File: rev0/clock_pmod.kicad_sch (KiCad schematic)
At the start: 5 parts, among them IC1 ECP5-BGA256, Y1 Osc60MHz

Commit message: hardware: use DNP field for DNP notation
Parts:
- TP1: DNP (none) -> DNP; Note DNP -> (none)
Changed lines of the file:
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@@
       (effects (font (size 1.27 1.27)) hide)
     )
-    (property "Note" "DNP" (id 4) (at 118.11 142.24 0)
+    (property "DNP" "DNP" (id 4) (at 118.11 142.24 0)
       (effects (font (size 1.27 1.27)) hide)
     )

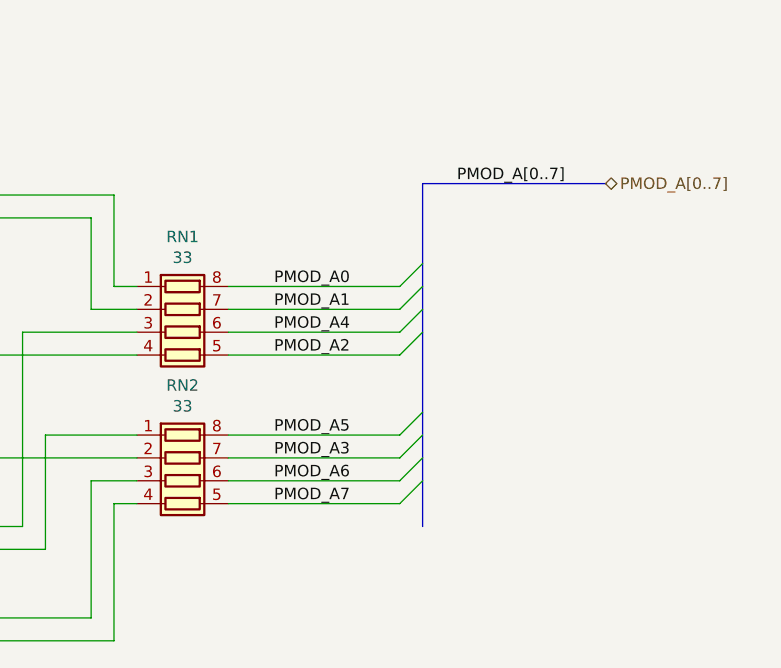
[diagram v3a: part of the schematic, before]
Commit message: hardware: reassign FPGA I/O banks
assign HyperRAM to DQS group
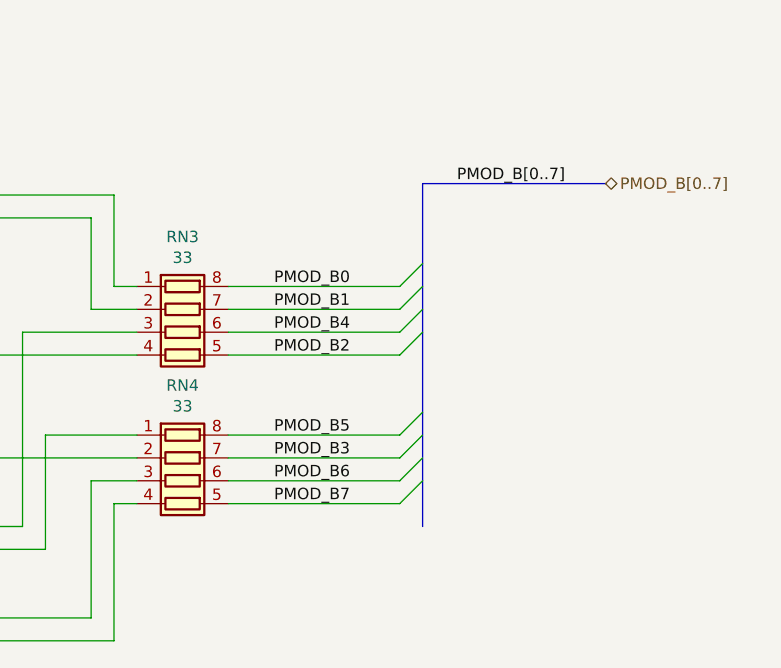
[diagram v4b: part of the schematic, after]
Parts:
- renumbered RN1 to RN3, RN2 to RN4
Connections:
- net PMOD_A0 renamed PMOD_B0
- net PMOD_A1 renamed PMOD_B1
- net PMOD_A2 renamed PMOD_B2
- net PMOD_A3 renamed PMOD_B3
- net PMOD_A4 renamed PMOD_B4
- net PMOD_A5 renamed PMOD_B5
- net PMOD_A6 renamed PMOD_B6
- net PMOD_A7 renamed PMOD_B7
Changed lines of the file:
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@@
     (stroke (width 0) (type default) (color 0 0 0 0))
   )
-  (label "PMOD_A3" (at 133.35 95.25 0)
-    (effects (font (size 1.27 1.27)) (justify left bottom))
-  )
-  (label "PMOD_A1" (at 133.35 78.74 0)
-    (effects (font (size 1.27 1.27)) (justify left bottom))
-  )
-  (label "PMOD_A2" (at 133.35 83.82 0)
-    (effects (font (size 1.27 1.27)) (justify left bottom))
-  )
-  (label "PMOD_A5" (at 133.35 92.71 0)
+  (label "PMOD_B3" (at 133.35 95.25 0)
+    (effects (font (size 1.27 1.27)) (justify left bottom))
+  )
+  (label "PMOD_B1" (at 133.35 78.74 0)
+    (effects (font (size 1.27 1.27)) (justify left bottom))
+  )
+  (label "PMOD_B2" (at 133.35 83.82 0)
+    (effects (font (size 1.27 1.27)) (justify left bottom))
+  )
+  (label "PMOD_B5" (at 133.35 92.71 0)
+    (effects (font (size 1.27 1.27)) (justify left bottom))
+  )
+  (label "PMOD_B[0..7]" (at 153.67 64.77 0)
     (effects (font (size 1.27 1.27)) (justify left bottom))
   )
@@
     (effects (font (size 1.27 1.27)) (justify left bottom))
   )
-  (label "PMOD_A0" (at 133.35 76.2 0)
-    (effects (font (size 1.27 1.27)) (justify left bottom))
-  )
-  (label "PMOD_A4" (at 133.35 81.28 0)
-    (effects (font (size 1.27 1.27)) (justify left bottom))
-  )
-  (label "PMOD_A7" (at 133.35 100.33 0)
-    (effects (font (size 1.27 1.27)) (justify left bottom))
-  )
-  (label "PMOD_A[0..7]" (at 153.67 64.77 0)
-    (effects (font (size 1.27 1.27)) (justify left bottom))
-  )
-  (label "PMOD_A6" (at 133.35 97.79 0)
-    (effects (font (size 1.27 1.27)) (justify left bottom))
-  )
-  (hierarchical_label "PMOD_A[0..7]" (shape bidirectional) (at 170.18 64.77 0)
+  (label "PMOD_B0" (at 133.35 76.2 0)
+    (effects (font (size 1.27 1.27)) (justify left bottom))
+  )
+  (label "PMOD_B4" (at 133.35 81.28 0)
+    (effects (font (size 1.27 1.27)) (justify left bottom))
+  )
+  (label "PMOD_B7" (at 133.35 100.33 0)
+    (effects (font (size 1.27 1.27)) (justify left bottom))
+  )
+  (label "PMOD_B6" (at 133.35 97.79 0)
+    (effects (font (size 1.27 1.27)) (justify left bottom))
+  )
+  (hierarchical_label "PMOD_B[0..7]" (shape bidirectional) (at 170.18 64.77 0)
     (effects (font (size 1.27 1.27)) (justify left))
   )
@@
   (symbol (lib_id "Device:R_Pack04") (at 123.19 81.28 270) (unit 1)
     (in_bom yes) (on_board yes)
-    (property "Reference" "RN1" (id 0) (at 123.19 70.6882 90))
+    (property "Reference" "RN3" (id 0) (at 123.19 70.6882 90))
     (property "Value" "33" (id 1) (at 123.19 72.9996 90))
     (property "Footprint" "Resistor_SMD:R_Array_Convex_4x0402" (id 2) (at 123.19 88.265 90)
@@
   (symbol (lib_id "Device:R_Pack04") (at 123.19 97.79 270) (unit 1)
     (in_bom yes) (on_board yes)
-    (property "Reference" "RN2" (id 0) (at 123.19 87.1982 90))
+    (property "Reference" "RN4" (id 0) (at 123.19 87.1982 90))
     (property "Value" "33" (id 1) (at 123.19 89.5096 90))
     (property "Footprint" "Resistor_SMD:R_Array_Convex_4x0402" (id 2) (at 123.19 104.775 90)

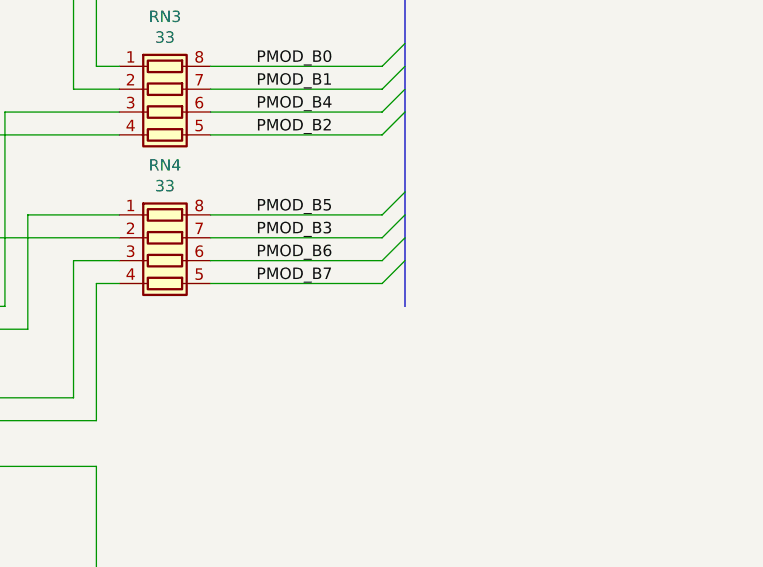
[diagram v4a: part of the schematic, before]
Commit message: hardware: rename USB ports
Sideband is renamed to Control and is intended for use as the primary
control port for both the FPGA and the microcontroller/debugger.

Host is renamed to Aux and is intended for auxiliary functions
including MitM.
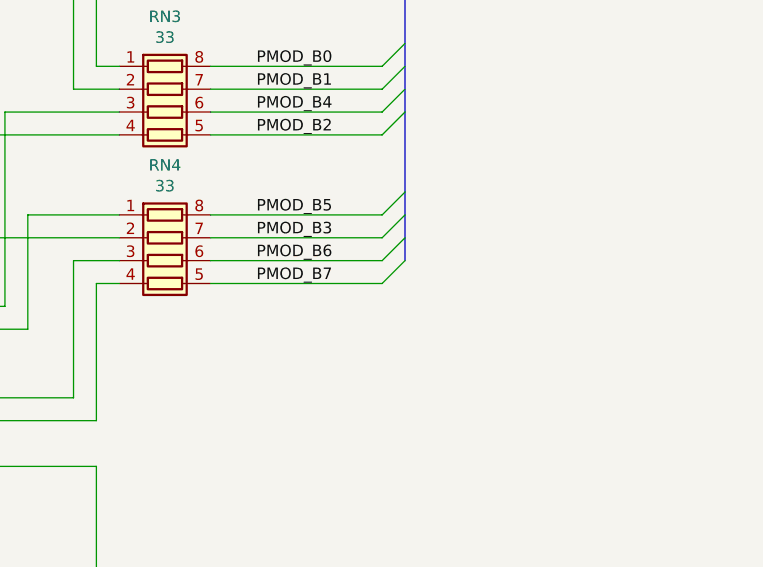
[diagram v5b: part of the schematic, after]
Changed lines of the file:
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@@
-    (stroke (width 0) (type default) (color 0 0 0 0))
-  )
-  (bus (pts (xy 149.86 97.79) (xy 149.86 102.87))
     (stroke (width 0) (type default) (color 0 0 0 0))
   )

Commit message: hardware: use "Exclude from bill of materials"
Virtual components such as mounting holes and test points that do not
require part placement now use this property instead of the DNP field.
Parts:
- TP1: DNP DNP -> (none); now left out of the parts list
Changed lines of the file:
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@@
   )
   (symbol (lib_id "Connector:TestPoint") (at 118.11 142.24 270) (unit 1)
-    (in_bom yes) (on_board yes)
+    (in_bom no) (on_board yes)
     (property "Reference" "TP1" (id 0) (at 121.1072 143.7132 0)
       (effects (font (size 1.27 1.27)) (justify left))
@@
       (effects (font (size 1.27 1.27)) hide)
     )
-    (property "DNP" "DNP" (id 4) (at 118.11 142.24 0)
-      (effects (font (size 1.27 1.27)) hide)
-    )
